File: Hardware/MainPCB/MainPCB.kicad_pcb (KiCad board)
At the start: 2 copper layers, 4 parts, among them Q1 FDS9926A, U1 BQ24075, U2 BQ29700

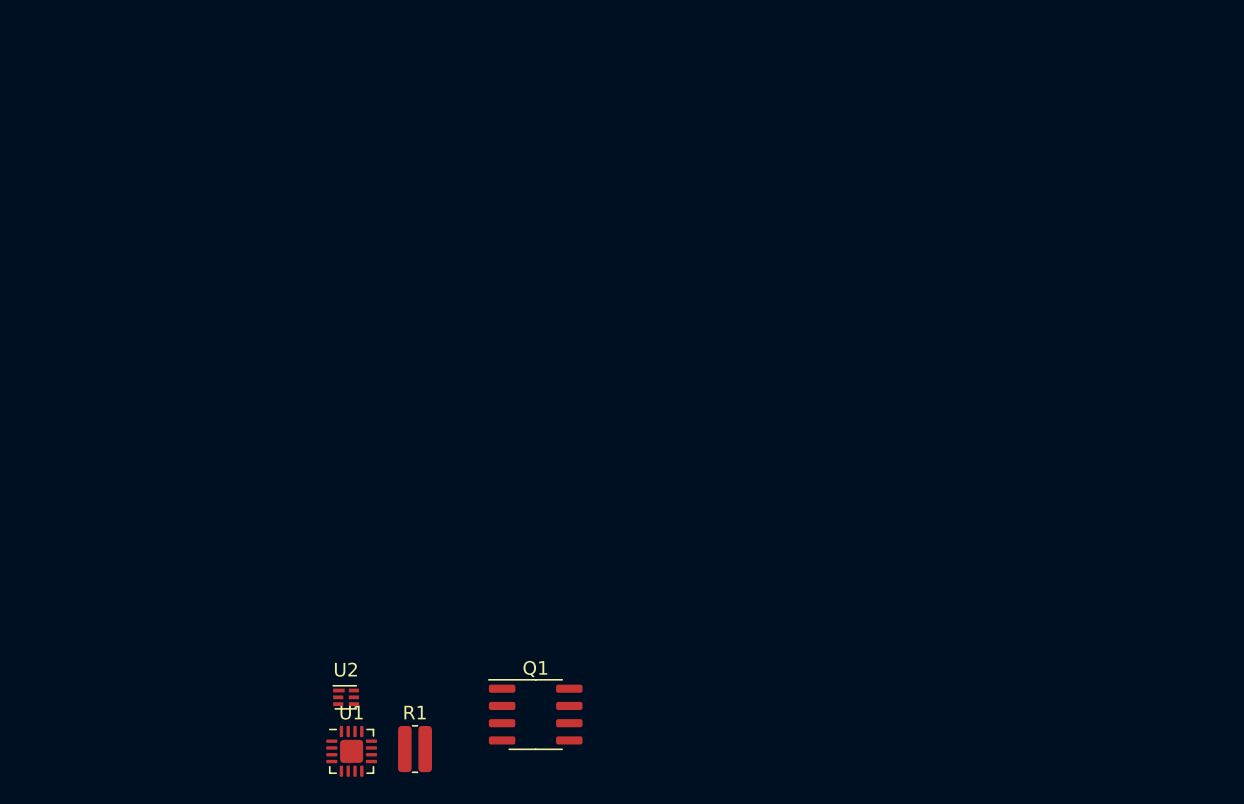
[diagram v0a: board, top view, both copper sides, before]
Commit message: Toevoeging 1 load switch
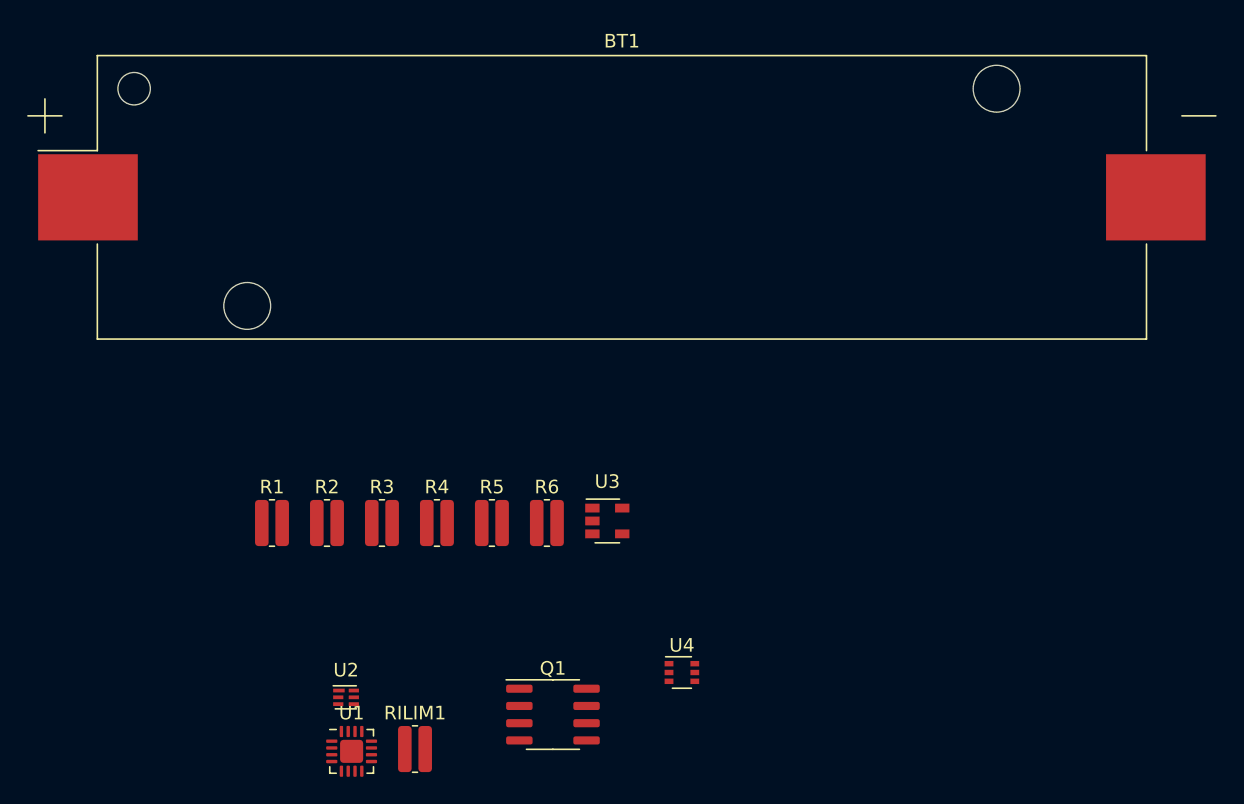
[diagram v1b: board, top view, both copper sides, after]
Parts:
- added BT1: Battery_Cell, Battery:BatteryHolder_Keystone_1042_1x18650, F.Cu at (127.0, 59.7)
- added R1: 680, Resistor_SMD:R_0612_1632Metric, F.Cu at (101.2, 83.7)
- added R2: 10k, Resistor_SMD:R_0612_1632Metric, F.Cu at (105.3, 83.7)
- added R3: 1.5k, Resistor_SMD:R_0612_1632Metric, F.Cu at (109.3, 83.7)
- added R4: 1.5k, Resistor_SMD:R_0612_1632Metric, F.Cu at (113.4, 83.7)
- added R5: 330, Resistor_SMD:R_0612_1632Metric, F.Cu at (117.4, 83.7)
- added R6: 2.2k, Resistor_SMD:R_0612_1632Metric, F.Cu at (121.5, 83.7)
- added U3: TLV75533PDBV, Package_TO_SOT_SMD:SOT-23-5, F.Cu at (125.9, 83.5)
- added U4: TPS22917DBV, Package_TO_SOT_SMD:SOT-363_SC-70-6, F.Cu at (131.4, 94.7)
- RILIM1: renamed from R1; value R -> 1.1k
- moved Q1 1.27 mm to (121.9, 97.8)
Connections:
- net Net-(U1-Pad13) renamed Vin
- Q1 pad 1: Net-(Q1-Pad1) -> VSS
- Q1 pad 3: Net-(Q1-Pad3) -> GND
- Q1 pad 7: Net-(Q1-Pad7) -> Net-(Q1-Pad5)
- Q1 pad 8: Net-(Q1-Pad7) -> Net-(Q1-Pad5)
- RILIM1 pad 1: Net-(R1-Pad1) (its old number) -> Net-(RILIM1-Pad1)
- RILIM1 pad 2: Net-(R1-Pad2) -> VSS
- U1 pad 10: Net-(U1-Pad10) -> VDD
- U1 pad 11: Net-(U1-Pad11) -> VDD
- U1 pad 12: Net-(U1-Pad12) -> Net-(RILIM1-Pad1)
- U1 pad 15: Net-(U1-Pad15) -> VSS
- U1 pad 17: Net-(U1-Pad17) -> VSS
- U1 pad 2: Net-(U1-Pad2) -> +BATT
- U1 pad 3: Net-(U1-Pad3) -> +BATT
- U1 pad 4: Net-(U1-Pad4) -> VSS
- U1 pad 5: Net-(U1-Pad5) -> VDD
- U1 pad 6: Net-(U1-Pad6) -> VSS
- U1 pad 8: Net-(U1-Pad8) -> VSS
- U2 pad 2: Net-(U2-Pad2) -> Net-(Q1-Pad4)
- U2 pad 3: Net-(U2-Pad3) -> Net-(Q1-Pad2)
- U2 pad 4: Net-(U2-Pad4) -> VSS

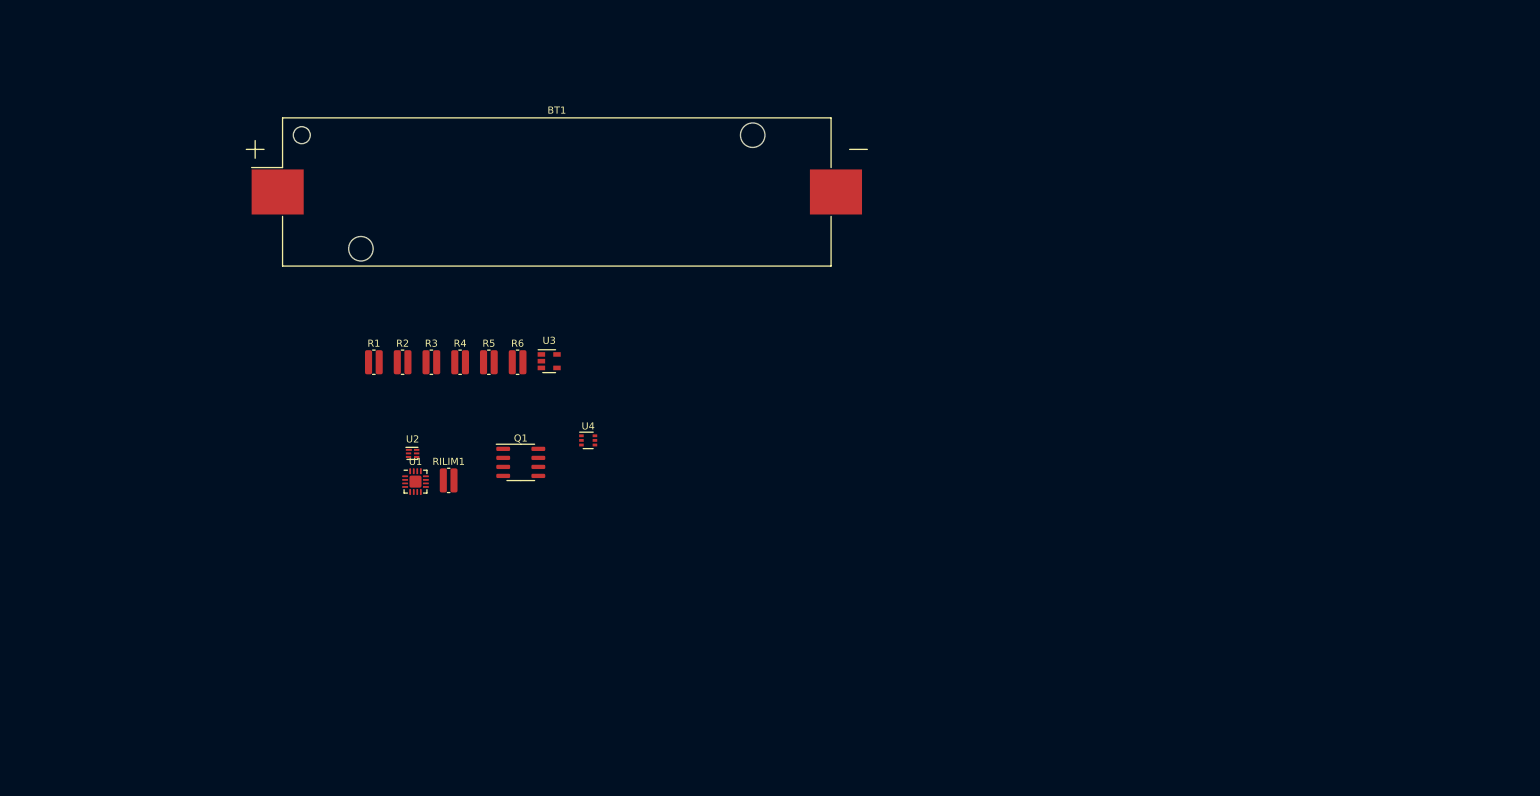
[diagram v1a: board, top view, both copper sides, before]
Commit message: schematic voor esp32 mainboard
de esp toegevoegd en de nodige connecties gemaakt
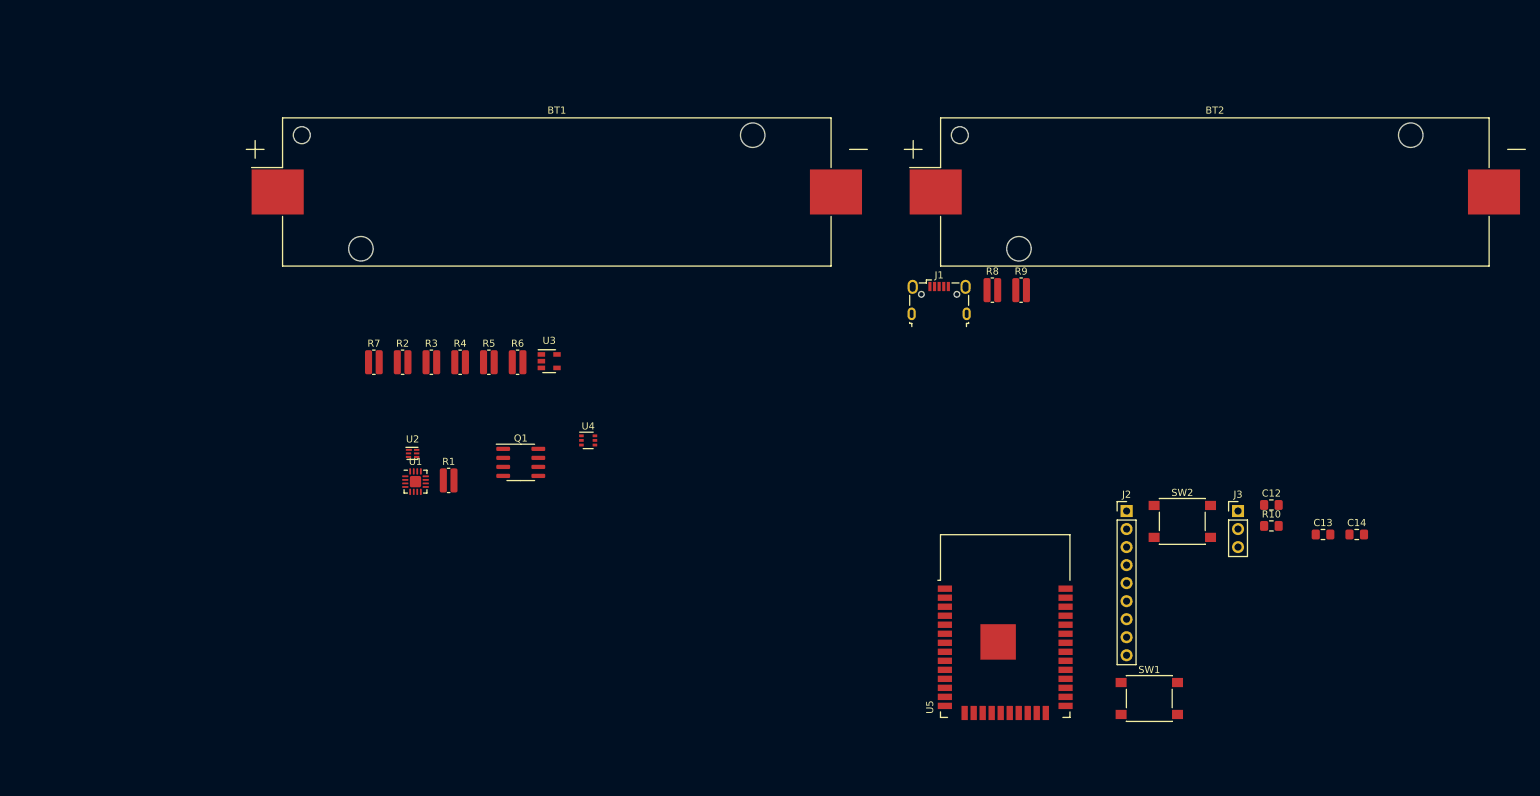
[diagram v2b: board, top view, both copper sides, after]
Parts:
- added BT2: Li-ion, Battery:BatteryHolder_Keystone_1042_1x18650, F.Cu at (219.7, 59.7)
- added C12: 100nF, Capacitor_SMD:C_0805_2012Metric_Pad1.15x1.40mm_HandSolder, F.Cu at (227.7, 103.8)
- added C13: 10µF, Capacitor_SMD:C_0805_2012Metric_Pad1.15x1.40mm_HandSolder, F.Cu at (234.9, 108.0)
- added C14: 100nF, Capacitor_SMD:C_0805_2012Metric_Pad1.15x1.40mm_HandSolder, F.Cu at (239.7, 108.0)
- added J1: USB_B_Micro, Connector_USB:USB_Micro-B_Wuerth_629105150521, F.Cu at (180.9, 74.9)
- added J2: Conn_01x09_Female, Connector_PinHeader_2.54mm:PinHeader_1x09_P2.54mm_Vertical, F.Cu at (207.3, 104.6)
- added J3: UART, Connector_PinHeader_2.54mm:PinHeader_1x03_P2.54mm_Vertical, F.Cu at (223.0, 104.6)
- added R10: 10k, Resistor_SMD:R_0805_2012Metric_Pad1.15x1.40mm_HandSolder, F.Cu at (227.7, 106.7)
- added R8: 5 Meg, Resistor_SMD:R_0612_1632Metric, F.Cu at (188.4, 73.5)
- added R9: 5 Meg, Resistor_SMD:R_0612_1632Metric, F.Cu at (192.4, 73.5)
- added SW1: SW_DIP_x01, Button_Switch_SMD:SW_Push_1P1T_NO_6x6mm_H9.5mm, F.Cu at (210.5, 131.1)
- added SW2: SW_DIP_x01, Button_Switch_SMD:SW_Push_1P1T_NO_6x6mm_H9.5mm, F.Cu at (215.1, 106.1)
- added U5: ESP32-WROOM-32D, RF_Module:ESP32-WROOM-32, F.Cu at (190.2, 123.8)
- BT1: value Battery_Cell -> Li-ion
- U1: footprint Package_DFN_QFN:QFN-16-1EP_3x3mm_P0.5mm_EP1.7x1.7mm -> Package_DFN_QFN:VQFN-16-1EP_3x3mm_P0.5mm_EP1.6x1.6mm
- U4: value TPS22917DBV -> TPS22919
- renumbered RILIM1 to R1, R1 to R7

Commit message: Main PCB volledig uitgerust met foorprints voor discrete componenten + BOM aangevuld met alles
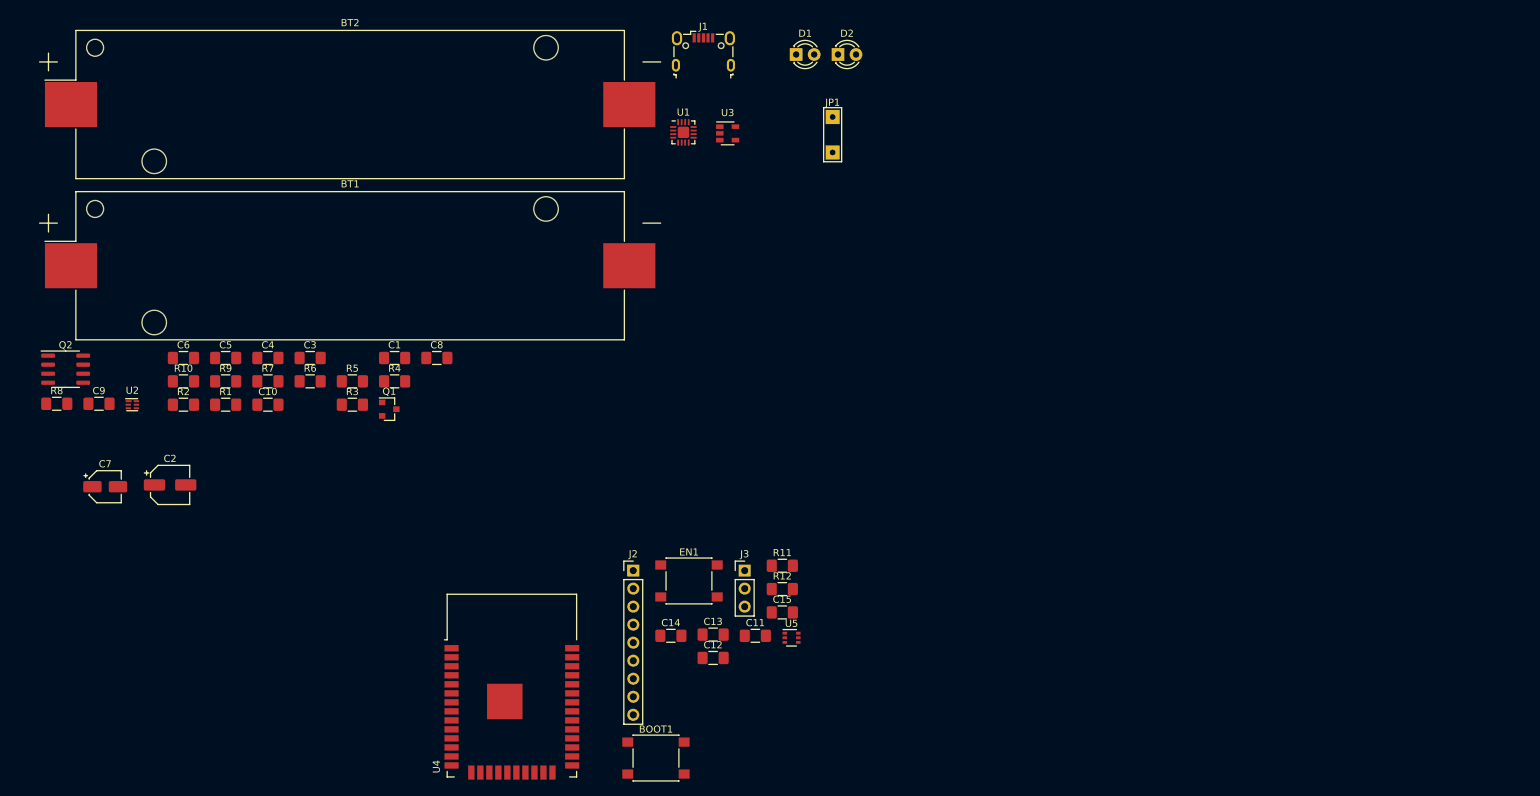
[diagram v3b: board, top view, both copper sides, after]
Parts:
- removed SW1, SW2: SW_DIP_x01, Button_Switch_SMD:SW_Push_1P1T_NO_6x6mm_H9.5mm
- added BOOT1: SW_DIP_x01, Button_Switch_SMD:SW_Push_1P1T_NO_6x6mm_H9.5mm, F.Cu at (141.0, 139.4)
- added C1: 1u, Capacitor_SMD:C_1206_3216Metric_Pad1.42x1.75mm_HandSolder, F.Cu at (104.1, 83.1)
- added C10: 47u, Capacitor_SMD:C_1206_3216Metric_Pad1.42x1.75mm_HandSolder, F.Cu at (86.3, 89.7)
- added C11: 100nF, Capacitor_SMD:C_1206_3216Metric_Pad1.42x1.75mm_HandSolder, F.Cu at (155.0, 122.2)
- added C15: 10u, Capacitor_SMD:C_1206_3216Metric_Pad1.42x1.75mm_HandSolder, F.Cu at (158.8, 118.9)
- added C2: 47u, Capacitor_SMD:CP_Elec_5x5.9, F.Cu at (72.5, 101.0)
- added C3: 1u, Capacitor_SMD:C_1206_3216Metric_Pad1.42x1.75mm_HandSolder, F.Cu at (92.2, 83.1)
- added C4: 4.7u, Capacitor_SMD:C_1206_3216Metric_Pad1.42x1.75mm_HandSolder, F.Cu at (86.3, 83.1)
- added C5: 4.7u, Capacitor_SMD:C_1206_3216Metric_Pad1.42x1.75mm_HandSolder, F.Cu at (80.3, 83.1)
- added C6: 1u, Capacitor_SMD:C_1206_3216Metric_Pad1.42x1.75mm_HandSolder, F.Cu at (74.4, 83.1)
- added C7: 47u, Capacitor_SMD:CP_Elec_4x5.4, F.Cu at (63.4, 101.2)
- added C8: 0.1u, Capacitor_SMD:C_1206_3216Metric_Pad1.42x1.75mm_HandSolder, F.Cu at (110.1, 83.1)
- added C9: 1u, Capacitor_SMD:C_1206_3216Metric_Pad1.42x1.75mm_HandSolder, F.Cu at (62.5, 89.5)
- added D1: LED_Green, LED_THT:LED_D3.0mm, F.Cu at (160.7, 40.3)
- added D2: LED_Blue, LED_THT:LED_D3.0mm, F.Cu at (166.6, 40.3)
- added EN1: SW_DIP_x01, Button_Switch_SMD:SW_Push_1P1T_NO_6x6mm_H9.5mm, F.Cu at (145.6, 114.5)
- added JP1: Jumper, Tobias_KiCad_Lib:Wire, F.Cu at (165.9, 51.6)
- added Q2: FDS9926A, Package_SO:SOIC-8_3.9x4.9mm_P1.27mm, F.Cu at (57.8, 84.7)
- added R11: 10k, Resistor_SMD:R_1206_3216Metric_Pad1.42x1.75mm_HandSolder, F.Cu at (158.8, 112.4)
- added R12: 680, Resistor_SMD:R_1206_3216Metric_Pad1.42x1.75mm_HandSolder, F.Cu at (158.8, 115.6)
- C12: value 100nF -> 10µF; footprint Capacitor_SMD:C_0805_2012Metric_Pad1.15x1.40mm_HandSolder -> Capacitor_SMD:C_1206_3216Metric_Pad1.42x1.75mm_HandSolder
- C13: value 10µF -> 100nF; footprint Capacitor_SMD:C_0805_2012Metric_Pad1.15x1.40mm_HandSolder -> Capacitor_SMD:C_1206_3216Metric_Pad1.42x1.75mm_HandSolder
- C14: value 100nF -> 1u; footprint Capacitor_SMD:C_0805_2012Metric_Pad1.15x1.40mm_HandSolder -> Capacitor_SMD:C_1206_3216Metric_Pad1.42x1.75mm_HandSolder
- Q1: value FDS9926A -> NTR2101P; footprint Package_SO:SOIC-8_3.9x4.9mm_P1.27mm -> Package_TO_SOT_SMD:SOT-23
- R1, R9: footprint Resistor_SMD:R_0612_1632Metric -> Resistor_SMD:R_1206_3216Metric_Pad1.42x1.75mm_HandSolder
- R10: value 10k -> 5 Meg; footprint Resistor_SMD:R_0805_2012Metric_Pad1.15x1.40mm_HandSolder -> Resistor_SMD:R_1206_3216Metric_Pad1.42x1.75mm_HandSolder
- R2: value 10k -> 47k; footprint Resistor_SMD:R_0612_1632Metric -> Resistor_SMD:R_1206_3216Metric_Pad1.42x1.75mm_HandSolder
- R3: value 1.5k -> 680; footprint Resistor_SMD:R_0612_1632Metric -> Resistor_SMD:R_1206_3216Metric_Pad1.42x1.75mm_HandSolder
- R4: value 1.5k -> 10k; footprint Resistor_SMD:R_0612_1632Metric -> Resistor_SMD:R_1206_3216Metric_Pad1.42x1.75mm_HandSolder
- R5: value 330 -> 1.5k; footprint Resistor_SMD:R_0612_1632Metric -> Resistor_SMD:R_1206_3216Metric_Pad1.42x1.75mm_HandSolder
- R6: value 2.2k -> 1.5k; footprint Resistor_SMD:R_0612_1632Metric -> Resistor_SMD:R_1206_3216Metric_Pad1.42x1.75mm_HandSolder
- R7: value 680 -> 330; footprint Resistor_SMD:R_0612_1632Metric -> Resistor_SMD:R_1206_3216Metric_Pad1.42x1.75mm_HandSolder
- R8: value 5 Meg -> 2.2k; footprint Resistor_SMD:R_0612_1632Metric -> Resistor_SMD:R_1206_3216Metric_Pad1.42x1.75mm_HandSolder
- U4: value TPS22919 -> ESP32-WROOM-32D; footprint Package_TO_SOT_SMD:SOT-363_SC-70-6 -> RF_Module:ESP32-WROOM-32
- U5: value ESP32-WROOM-32D -> TPS22919; footprint RF_Module:ESP32-WROOM-32 -> Package_TO_SOT_SMD:SOT-363_SC-70-6
- moved R10 154.6 mm to (74.4, 86.4)
- moved R8 132.8 mm to (56.5, 89.5)
- moved BT2 122.5 mm to (97.9, 47.4)
- moved R9 112.8 mm to (80.3, 86.4)
- moved C14 97.7 mm to (143.1, 122.2)
- moved C13 87.1 mm to (149.0, 122.1)
- moved C12 81.6 mm to (149.0, 125.3)
- moved J2 70.0 mm to (137.8, 113.0)
- moved J3 70.0 mm to (153.5, 113.0)
- moved U1 62.0 mm to (144.8, 51.3)
- moved J1 48.3 mm to (147.7, 39.9)
- moved U3 40.8 mm to (151.1, 51.4)
- moved U2 40.1 mm to (67.2, 89.7)
- moved U4 39.0 mm to (120.7, 132.2)
- moved R1 33.2 mm to (80.3, 89.7)
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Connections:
- BT1 pad 2: VSS -> Net-(BT1-Pad2)
- BT2 pad 2: VSS -> Net-(BT1-Pad2)
- C12 pad 1: Net-(C12-Pad1) -> GND
- C12 pad 2: GND -> +3V3
- C13 pad 1: GND -> +3V3
- C13 pad 2: +3V3 -> GND
- Q1 pad 2: Net-(Q1-Pad2) -> VDD1
- Q1 pad 3: GND -> +BATT
- R10 pad 1: +3V3 -> Net-(Q2-Pad4)
- R10 pad 2: Net-(C12-Pad1) -> VSS
- R3 pad 1: VDD -> Net-(R3-Pad1)
- R3 pad 2: Net-(D1-Pad2) -> VSS
- R4 pad 1: VDD -> Net-(R4-Pad1)
- R4 pad 2: Net-(D2-Pad2) -> VSS
- R5 pad 1: +BATT -> VDD2
- R5 pad 2: Net-(C7-Pad1) -> Net-(D1-Pad2)
- R6 pad 1: Net-(R6-Pad1) -> VDD2
- R6 pad 2: VSS -> Net-(D2-Pad2)
- R7 pad 1: Net-(R7-Pad1) -> VDD1
- R7 pad 2: VSS -> Net-(C8-Pad1)
- R8 pad 1: Net-(Q1-Pad4) -> Net-(R8-Pad1)
- R8 pad 2: GND -> VSS
- R9 pad 1: Net-(Q1-Pad2) -> Net-(Q2-Pad2)
- R9 pad 2: VSS -> GND
- U1 pad 1: Net-(R2-Pad1) -> Net-(R4-Pad1)
- U1 pad 10: VDD -> VDD2
- U1 pad 11: VDD -> VDD2
- U1 pad 14: Net-(U1-Pad14) -> Net-(R2-Pad1)
- U1 pad 16: Net-(R7-Pad1) -> Net-(R3-Pad1)
- U1 pad 2: +BATT -> VDD1
- U1 pad 3: +BATT -> VDD1
- U1 pad 5: VDD -> VDD2
- U2 pad 2: Net-(Q1-Pad4) -> Net-(Q2-Pad2)
- U2 pad 3: Net-(Q1-Pad2) -> Net-(Q2-Pad4)
- U2 pad 5: Net-(C7-Pad1) -> Net-(C8-Pad1)
- U2 pad 6: Net-(R6-Pad1) -> Net-(R8-Pad1)
- U3 pad 1: VDD -> VDD2
- U3 pad 3: VDD -> VDD2
- U4 pad 1: +3V3 -> GND
- U4 pad 2: GND -> +3V3
- U4 pad 6: Net-(C15-Pad1) -> AUX
- U5 pad 1: GND -> +3V3
- U5 pad 2: +3V3 -> GND
- U5 pad 3: Net-(C12-Pad1) -> Net-(U5-Pad3)
- U5 pad 6: AUX -> Net-(C15-Pad1)
